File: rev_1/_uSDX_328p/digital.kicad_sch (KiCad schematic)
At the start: 2 parts

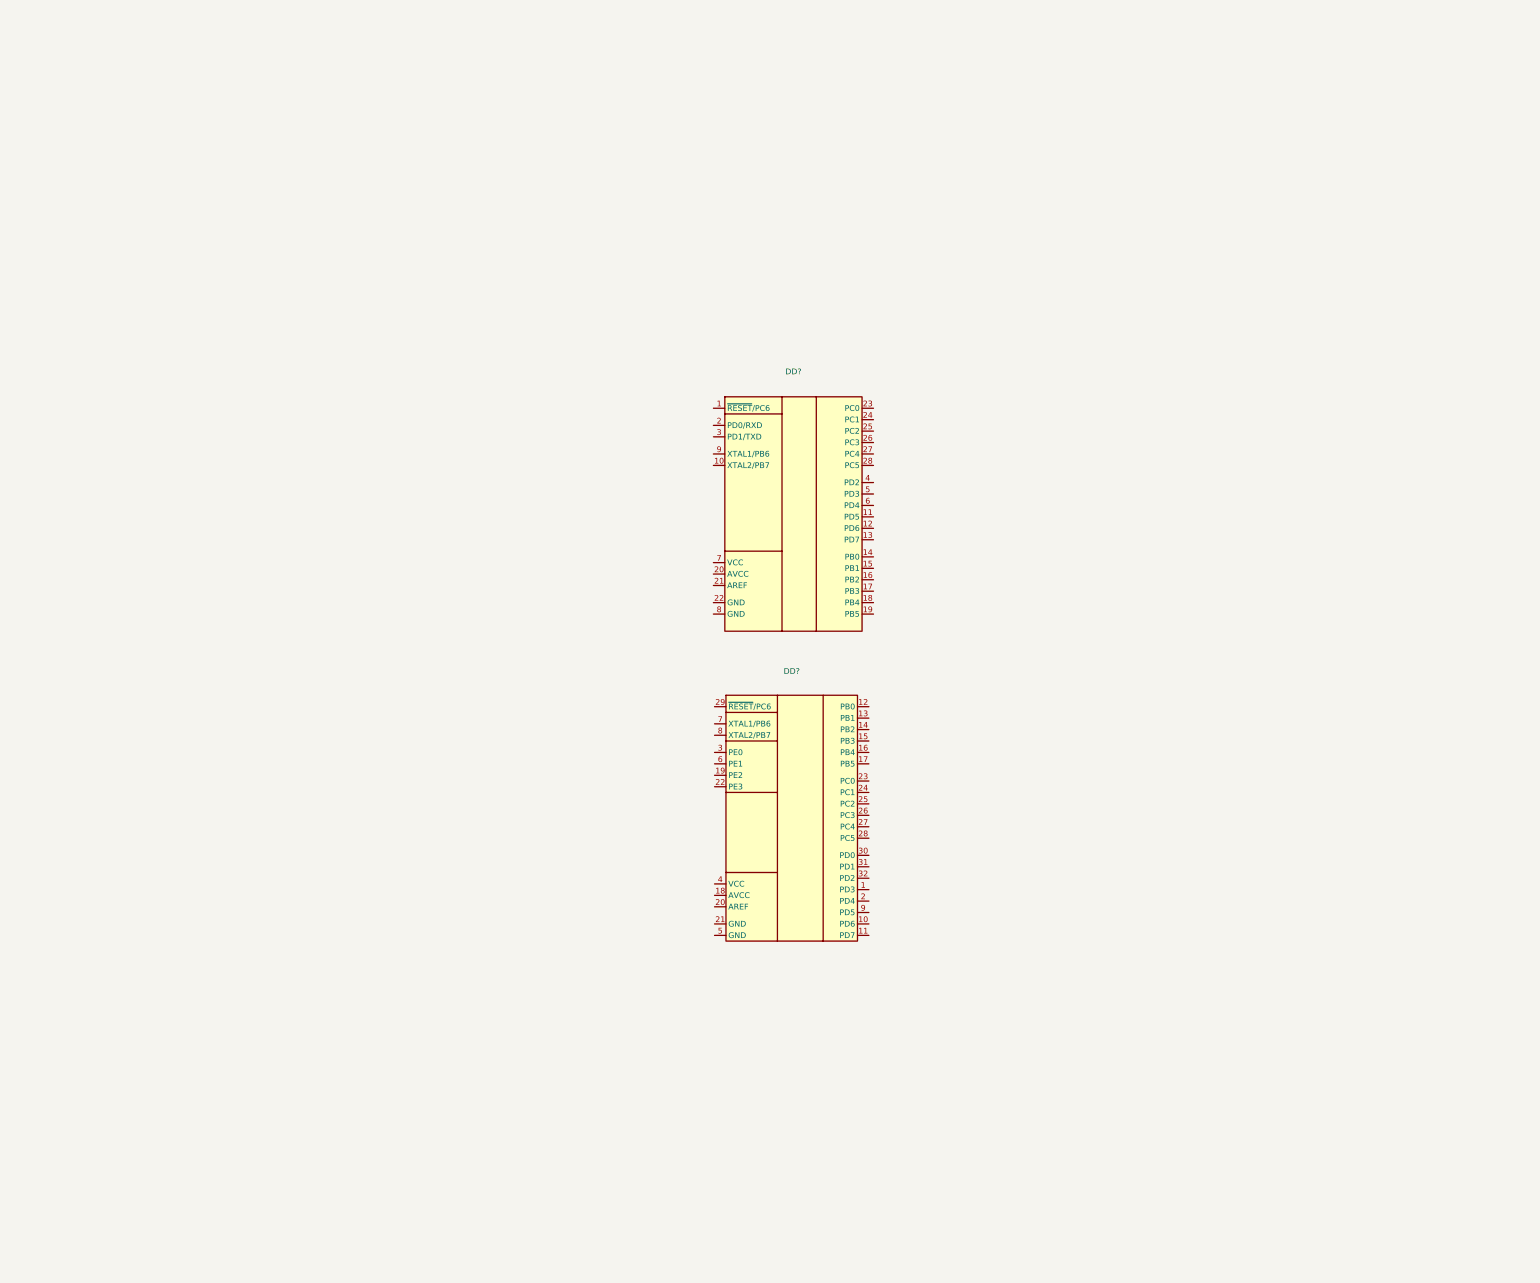
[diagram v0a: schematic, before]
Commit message: Добавил si5351 и энкодер
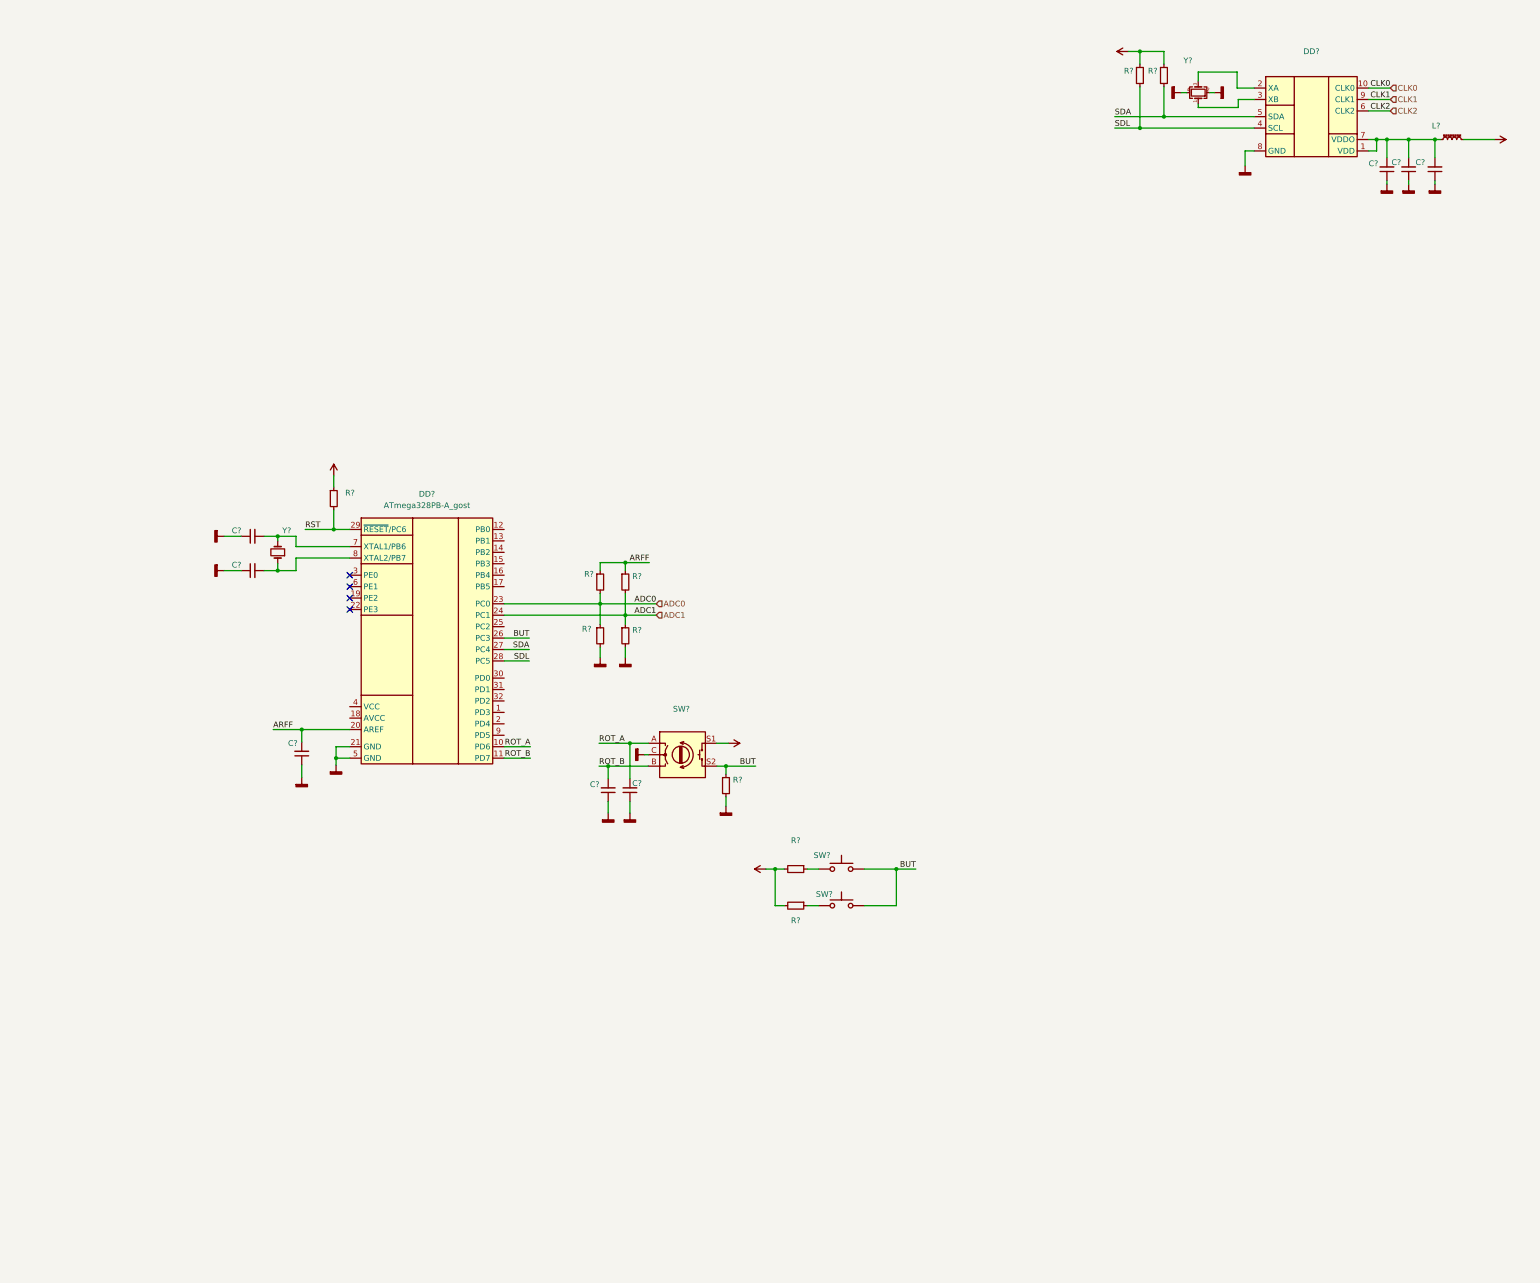
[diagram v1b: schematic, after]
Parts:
- removed DD?: (no value), symbol MCU_Microchip_ATmega:ATmega48PV-10P_gost
- added C? (x8): (no value), symbol Device:C_Small
- added DD?: (no value), Package_SO:MSOP-10_3x3mm_P0.5mm, symbol Oscillator:Si5351A-B-GT_gost
- added L?: (no value), symbol Device:L_Ferrite_Small
- added R? (x10): (no value), symbol Device:R_Small
- added SW? (x2): (no value), symbol Switch:SW_Push
- added SW?: (no value), symbol Device:RotaryEncoder_Switch
- added Y?: (no value), symbol Device:Crystal_GND24_Small
- added Y?: (no value), symbol Device:Crystal_Small
- DD?: value (none) -> ATmega328PB-A_gost; footprint (none) -> Package_QFP:TQFP-32_7x7mm_P0.8mm
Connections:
- net ROT_A: now reaches DD?.10 (PD6)
- net ROT_A: now also C?.2, SW?.A
- net ROT_B: now reaches DD?.11 (PD7)
- net ROT_B: now also C?.2, SW?.B
- net ARFF: now reaches DD?.20 (AREF)
- net ARFF: now also C?.2, R?.1, R?.1
- net GNDD: now reaches DD?.21 (GND)
- net GNDD: now also DD?.5 (GND), C?.1, C?.1, C?.1, C?.1, C?.1, C?.1, C?.1, C?.1, DD?.8 (GND), R?.2, R?.2, R?.2, SW?.C, Y?.2, Y?.4
- net ADC0: now reaches DD?.23 (PC0)
- net ADC0: now also R?.1, R?.2
- net ADC1: now reaches DD?.24 (PC1)
- net ADC1: now also R?.1, R?.2
- net BUT: now reaches DD?.26 (PC3)
- net BUT: now also R?.1, SW?.2, SW?.2, SW?.S2
- net SDA: now reaches DD?.27 (PC4)
- net SDA: now also DD?.5 (SDA), R?.2
- net SDL: now reaches DD?.28 (PC5)
- net SDL: now also DD?.4 (SCL), R?.2
- net RST: now reaches DD?.29 (~{RESET}/PC6)
- net RST: now also R?.2
- net at DD?.7 (XTAL1/PB6): now also C?.2, Y?.2
- net at DD?.8 (XTAL2/PB7): now also C?.2, Y?.1
- new net: C?.2, C?.2, C?.2, DD?.1 (VDD), DD?.7 (VDDO), L?.1
- new net: DD?.2 (XA), Y?.3
- new net: DD?.3 (XB), Y?.1
- new net: R?.1, SW?.1 (x2)
- new net +3V3: L?.2, R?.1, R?.1
- new net +5V: R?.1, R?.2, R?.2, SW?.S1
- new net CLK0: DD?.10 (CLK0)
- new net CLK1: DD?.9 (CLK1)
- new net CLK2: DD?.6 (CLK2)
- no-connect marks 0 -> 4
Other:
- company: (none) -> hamradio@conference.jabber.ru
- title: (none) -> uSDX_328P Трансивер
- moved on the sheet: DD?

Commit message: Добавил разъем для подключения экрана LCD1602,согласовал уровни к i2c  и добавил преобразователь CP2102 для подключения к компьютеру
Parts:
- added C? (x4): (no value), symbol Device:C_Small
- added D1: (no value), symbol Power_Protection:SP0503BAHT
- added DD?: (no value), symbol cel366_gost_ic:CP2102
- added J1: (no value), symbol Connector:USB_B_Mini
- added LD?: (no value), symbol Device:LED_Small
- added Q?: BC847, Package_TO_SOT_SMD:SOT-23, symbol Transistor_BJT:BC847
- added Q?: BSS138, Package_TO_SOT_SMD:SOT-23, symbol Transistor_FET:BSS138
- added Q?: ~, symbol Transistor_FET:BSS138
- added R? (x2): NC, symbol Device:R_Small
- added R? (x4): (no value), symbol Device:R_Small
- added R? (x2): 4K7, symbol Device:R_Small
- added R?: 10K, symbol Device:R_Small
- added R?: 2K, symbol Device:R_Small
- added RV?: 10K, symbol Device:R_Potentiometer_Small
- added XP?: LCD 1602, symbol Connector:Conn_01x16_Female_gost
- C? (x4): value (none) -> 0.1u
- C?: value (none) -> 1uF
- C? (x2): value (none) -> 22p
- C?: value (none) -> 4.7u
- DD?: value (none) -> Si5351A-B-GT_gost
- L?: value (none) -> BLM18EG221SN1D
- R? (x6): value (none) -> 10K
- R? (x2): value (none) -> 4K7
- R?: value (none) -> 3K3
- R?: value (none) -> 1K
- SW?: value (none) -> L_BUTT
- SW?: value (none) -> R_BUTT
- SW?: value (none) -> RotaryEncoder_Switch
- Y?: value (none) -> 27MHz
- Y?: value (none) -> 20MHz
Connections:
- net +3V3: now also Q?.1 (G), Q?.1 (G)
- net +5V: now also R?.1, R?.2, R?.2, RV?.1, XP?.15 (Pin_15), XP?.2 (Pin_2)
- net GNDD: now also C?.1, C?.1, C?.2, C?.2, D1.1 (A), DD?.29 (PAD), DD?.3 (GND), J1.5 (GND), J1.6 (Shield), LD?.1 (K), Q?.2 (E), R?.2, R?.2, R?.2, RV?.3, XP?.1 (Pin_1), XP?.5 (Pin_5)
- net SDA: now also Q?.3 (D), R?.1; no longer DD?.5 (SDA), R?.2
- net SDL: now also Q?.3 (D), R?.1; no longer DD?.4 (SCL), R?.2
- net DB5: now reaches DD?.1 (PD3)
- net DB5: now also XP?.12 (Pin_12)
- net LED_ON: now reaches DD?.19 (PE2)
- net LED_ON: now also R?.2
- net DB6: now reaches DD?.2 (PD4)
- net DB6: now also XP?.13 (Pin_13)
- net E: now reaches DD?.3 (PE0)
- net E: now also XP?.6 (Pin_6)
- net RX: now reaches DD?.30 (PD0)
- net RX: now also R?.2
- net TX: now reaches DD?.31 (PD1)
- net TX: now also R?.2
- net DB4: now reaches DD?.32 (PD2)
- net DB4: now also XP?.11 (Pin_11)
- net RS: now reaches DD?.6 (PE1)
- net RS: now also XP?.4 (Pin_4)
- net DB7: now reaches DD?.9 (PD5)
- net DB7: now also XP?.14 (Pin_14)
- new net: R?.1, R?.2, RV?.2, XP?.3 (Pin_3)
- new net: DD?.11 (~{SUSPEND}), R?.1
- new net: LD?.2 (A), R?.2
- new net: DD?.4 (SCL), Q?.2 (S), R?.2
- new net: DD?.5 (SDA), Q?.2 (S), R?.2
- new net: DD?.12 (SUSPEND), R?.1
- new net: DD?.26 (TXD), R?.1
- new net: Q?.1 (B), R?.1, R?.1
- new net: DD?.25 (RXD), R?.1
- new net: Q?.3 (C), XP?.16 (Pin_16)
- new net USB_D+: D1.3 (K), DD?.4 (D+), J1.3 (D+)
- new net USB_D-: D1.4 (K), DD?.5 (D-), J1.2 (D-)
- new net VBUS: C?.2, C?.2, D1.2 (K), DD?.7 (REGIN), DD?.8 (VBUS), J1.1 (VBUS)
- new net VCC: C?.1, C?.1, DD?.6 (VDD)
- no-connect marks 4 -> 23
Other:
- note added: "BG_GND"
- note added: "BG_VCC"
- note added: "DB0"
- note added: "DB1"
- note added: "DB2"
- note added: "DB3"
- note added: "DB4"
- note added: "DB5"
- note added: "DB6"
- note added: "DB7"
- note added: "E"
- note added: "GND"
- note added: "RS"
- note added: "RW"
- note added: "USB detect"
- note added: "VCC"
- note added: "VO"
- note added: "Можно отрегулировать перменным резистором и запаять постоянные"
- moved on the sheet: C?, DD?, L?, R?, SW?, Y?

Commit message: Добавил расширитель GPIO PCA9550 для перключения фильтров и подключения кнопок быстрой настройки (просил U2)
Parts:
- added C?: 0.1mF, symbol Device:C_Small
- added DD?: PCA9555DB_gost, Package_SO:SSOP-24_5.3x8.2mm_P0.65mm, symbol Interface_Expansion:PCA9555DB_gost
- added JP? (x3): ~, symbol Jumper:Jumper_2_Open
- added R? (x11): 4K7, symbol Device:R_Small
- added SW? (x4): +, symbol Switch:SW_Push
- added SW? (x4): -, symbol Switch:SW_Push
- C? (x2): value (none) -> 0.1mF
- C? (x2): value (none) -> 10mF
- D1: value (none) -> SP0503BAHT; footprint (none) -> Package_TO_SOT_SMD:SOT-143
- DD?: value (none) -> CP2102-GM; footprint (none) -> Package_DFN_QFN:QFN-28-1EP_5x5mm_P0.5mm_EP3.35x3.35mm_ThermalVias
- J1: value (none) -> USB_B_Mini
- LD?: value (none) -> TX
- R? (x2): value (none) -> 330R
- R?: value (none) -> 10K
- R?: value (none) -> 300R
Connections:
- net +5V: now also C?.1, DD?.24 (VDD), R?.1, R?.1, R?.1, R?.1, R?.1, R?.1, R?.1, R?.1, R?.1, R?.1, R?.1
- net GNDD: now also C?.2, DD?.12 (GND), JP?.1 (A), JP?.1 (A), JP?.1 (A), SW?.2, SW?.2, SW?.2, SW?.2, SW?.2, SW?.2, SW?.2, SW?.2
- net SDA: now also DD?.23 (SDA)
- net SDL: now also DD?.22 (SCL)
- net INT: now reaches DD?.22 (PE3)
- net INT: now also DD?.1 (~{INT})
- new net: DD?.21 (A0), JP?.2 (B), R?.2
- new net: DD?.2 (A1), JP?.2 (B), R?.2
- new net: DD?.3 (A2), JP?.2 (B), R?.2
- new net BUT_1: DD?.5 (IO0_1), R?.2, SW?.1
- new net BUT_2: DD?.6 (IO0_2), R?.2, SW?.1
- new net BUT_3: DD?.7 (IO0_3), R?.2, SW?.1
- new net BUT_4: DD?.8 (IO0_4), R?.2, SW?.1
- new net BUT_5: DD?.9 (IO0_5), R?.2, SW?.1
- new net BUT_6: DD?.10 (IO0_6), R?.2, SW?.1
- new net BUT_7: DD?.11 (IO0_7), R?.2, SW?.1
- new net BUT_8: DD?.13 (IO1_0), R?.2, SW?.1
- new net IO0_0: DD?.4 (IO0_0)
- new net IO1_1: DD?.14 (IO1_1)
- new net IO1_2: DD?.15 (IO1_2)
- new net IO1_3: DD?.16 (IO1_3)
- new net IO1_4: DD?.17 (IO1_4)
- new net IO1_5: DD?.18 (IO1_5)
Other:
- note added: "Блок кнопок для быстрой настройки просил U2"

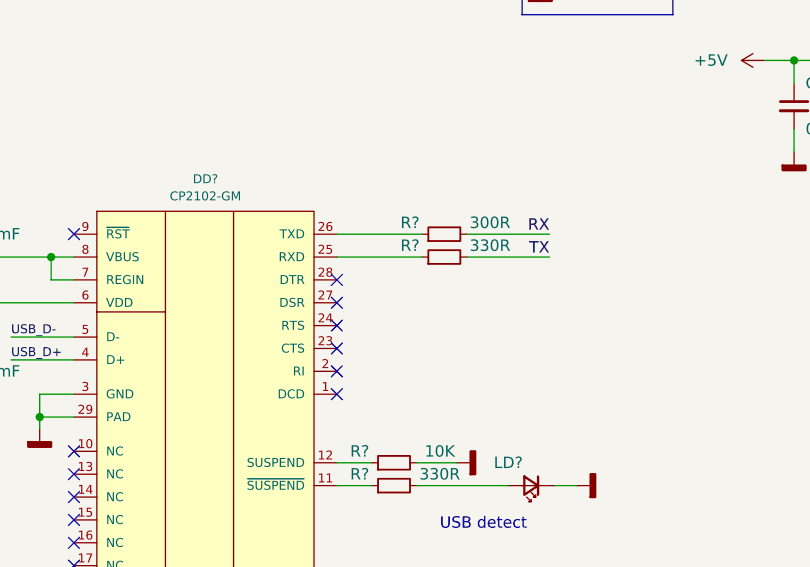
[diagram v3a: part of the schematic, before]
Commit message: Добавил управление линией сброса CP2102 для прошивки из среды Arduino
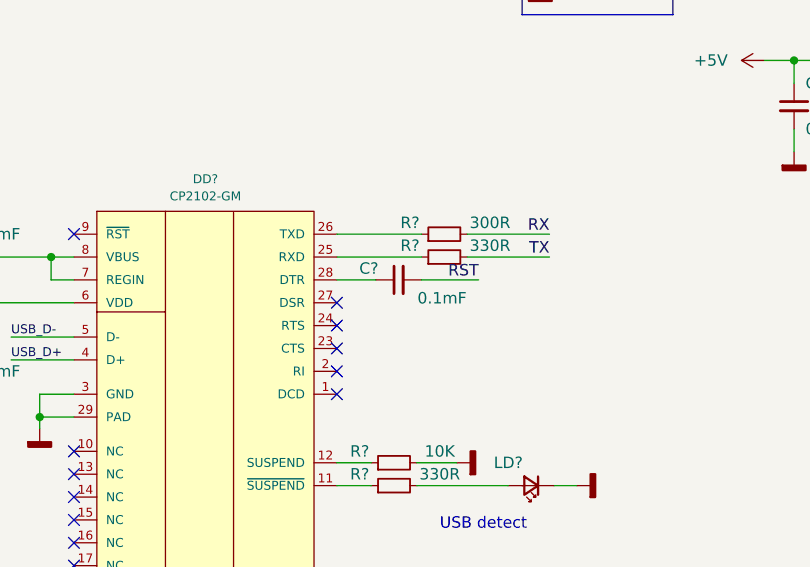
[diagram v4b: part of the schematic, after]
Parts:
- added C?: 0.1mF, symbol Device:C_Small
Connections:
- net RST: now also C?.2
- net at DD?.28 (DTR): now also C?.1
- no-connect marks 23 -> 22
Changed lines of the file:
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@@
   )
   (no_connect (at 104.902 106.934))
-  (no_connect (at 104.902 101.854))
   (no_connect (at 75.692 123.444))
   (no_connect (at 75.692 125.984))
@@
     (stroke (width 0) (type default) (color 0 0 0 0))
   )
+  (wire (pts (xy 114.3 101.854) (xy 120.65 101.854))
+    (stroke (width 0) (type default) (color 0 0 0 0))
+  )
   (wire (pts (xy 272.288 56.896) (xy 275.844 56.896))
     (stroke (width 0) (type default) (color 0 0 0 0))
@@
   )
   (wire (pts (xy 327.406 33.02) (xy 327.406 34.798))
+    (stroke (width 0) (type default) (color 0 0 0 0))
+  )
+  (wire (pts (xy 104.902 101.854) (xy 109.22 101.854))
     (stroke (width 0) (type default) (color 0 0 0 0))
   )
@@
   )
   (label "TX" (at 142.24 232.918 180)
+    (effects (font (size 1.27 1.27)) (justify right bottom))
+  )
+  (label "RST" (at 120.65 101.854 180)
     (effects (font (size 1.27 1.27)) (justify right bottom))
   )
@@
     (pin "1")
   )
+  (symbol (lib_id "Device:C_Small") (at 111.76 101.854 90) (unit 1)
+    (in_bom yes) (on_board yes)
+    (property "Reference" "C?" (id 0) (at 108.458 100.584 90))
+    (property "Value" "0.1mF" (id 1) (at 116.586 103.886 90))
+    (property "Footprint" "" (id 2) (at 111.76 101.854 0)
+      (effects (font (size 1.27 1.27)) hide)
+    )
+    (property "Datasheet" "~" (id 3) (at 111.76 101.854 0)
+      (effects (font (size 1.27 1.27)) hide)
+    )
+    (pin "1")
+    (pin "2")
+  )
   (symbol (lib_id "Switch:SW_Push") (at 336.296 24.892 0) (unit 1)
